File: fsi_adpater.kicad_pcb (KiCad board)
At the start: 2 copper layers, 16.8 x 25.7 mm, 8 parts, among them IC1 74AVC4TD245PW,118, J1 QTH-030-01-F-D-A-K, J2 Conn_01x05, J3 Conn_01x03, U1 TLV73311PDBV

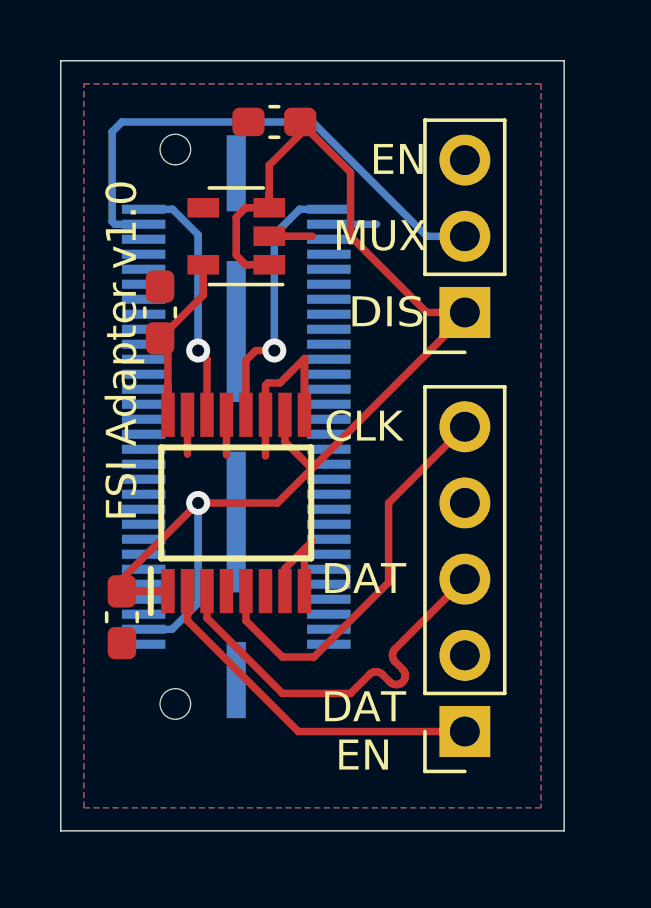
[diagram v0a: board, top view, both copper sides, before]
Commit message: fsi-adapter: v1.1: Shift 3pin connector away from 5pin.
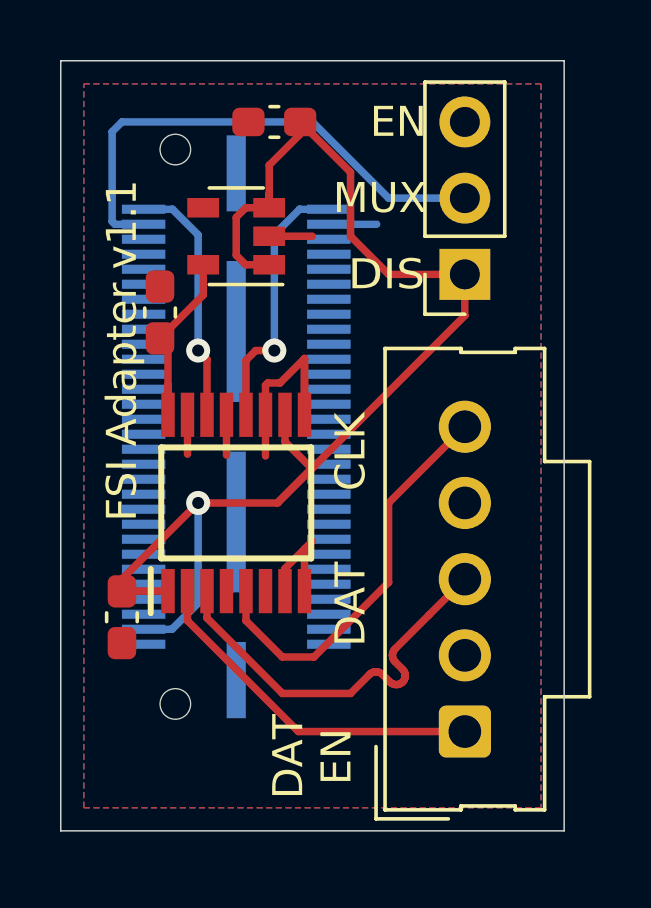
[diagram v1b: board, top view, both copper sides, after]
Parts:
- J2: value Conn_01x05 -> 1719710003; footprint Connector_PinSocket_2.54mm:PinSocket_1x05_P2.54mm_Vertical -> parts:Molex_SL_171971-0005_1x05_P2.54mm_Vertical
- moved J3 1.27 mm to (44.5, 34.3)
- turned J2 to 90 degrees
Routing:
- net +3V3: track 41.8 -> 44.3 mm
- net /DBG_MUX_SEL: track 17.6 -> 17.0 mm
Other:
- board text added: "FSI Adapter v1.1"
- board text removed: "FSI Adapter v1.0"
